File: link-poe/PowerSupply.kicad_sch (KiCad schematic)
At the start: 8 parts, among them U501 TPSM33625RDNR

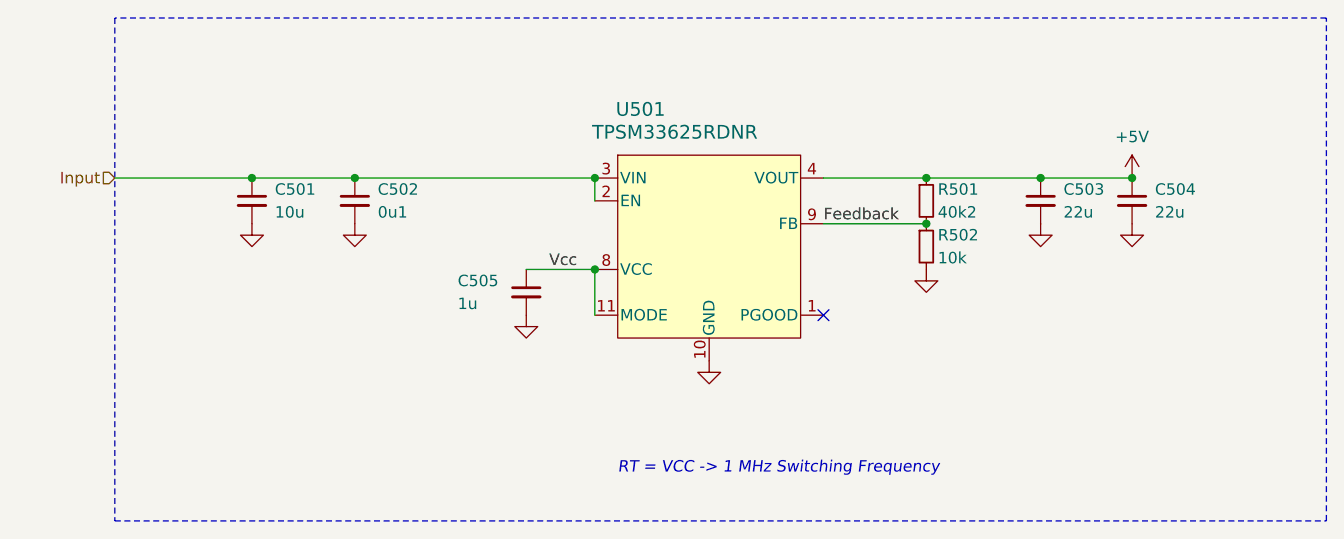
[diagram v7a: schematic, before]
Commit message: Replace Order_Number
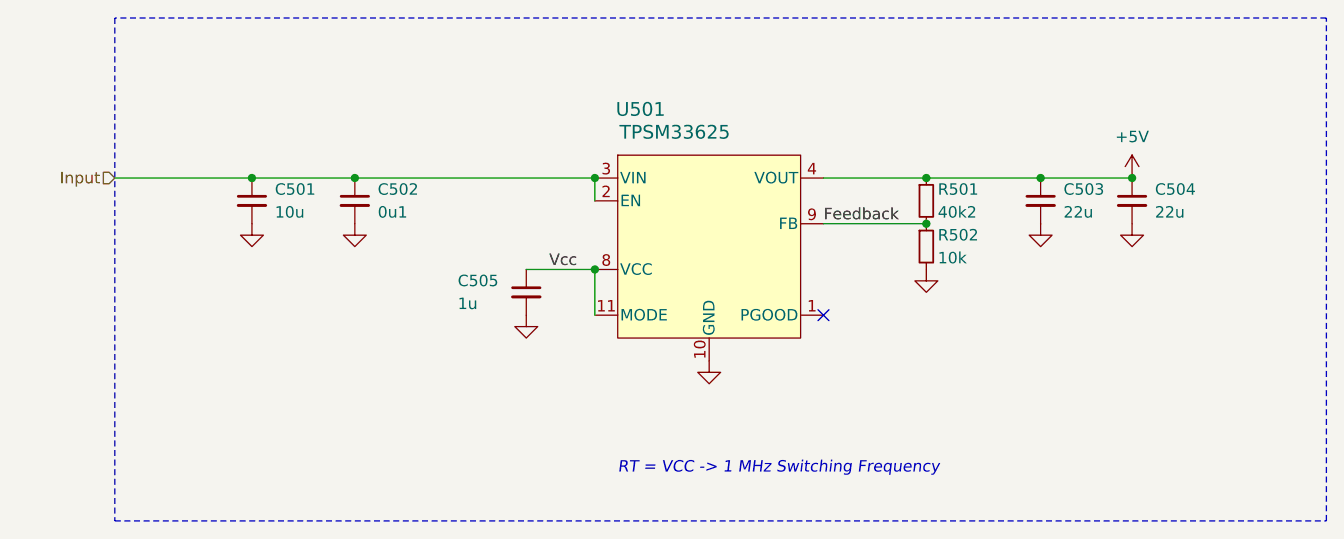
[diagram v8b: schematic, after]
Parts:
- U501: value TPSM33625RDNR -> TPSM33625
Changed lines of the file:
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@@
 			)
 		)
-		(property "Value" "TPSM33625RDNR"
+		(property "Value" "TPSM33625"
 			(at 144.78 90.17 0)
 			(effects
